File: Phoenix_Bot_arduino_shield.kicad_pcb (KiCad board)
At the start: 2 copper layers, 135.9 x 64.8 mm, 46 parts, among them J1 Analog_signal_male, J10 Ground, J11 Ground, J12 Ground, J13 12V_terminal, J14 PWN(10-5), J15 On Board Supply, J16 1x8 Male, J17 1x8 Male, J18 PWM_(6-1), J19 Analog_Pin_1, J2 Encoder_signal, J20 1x8 Female, J21 1x8 Female, J22 Serial, J23 ICSP, J24 Analog_Pin_2, J25 Digital_Pins, J27 Solenoid_terminal, J28 Solendoid_middle_terminal, J29 bottom_solenoid_terminal, J3 Servo_signal, J4 Analog_signal_female, J5 Analog_signal_power, J6 Servo_Power, J7 Encoder_Power, J8 Analog_Power_female, J9 Ground, q1 solenoid_1, q2 solenoid_4, q3 solenoid_3, q4 solenoid_5, q5 solenoid_3, q6 solenoid_6

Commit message: Added .gitignore, rescued old PCB file. Cleaned up repo to match .gitignore settings.
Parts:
- removed J10, J11: Ground, Pin_Headers:Pin_Header_Straight_1x06_Pitch2.54mm
- removed J12, J9: Ground, Pin_Headers:Pin_Header_Straight_1x08_Pitch2.54mm
- removed J5: Analog_signal_power, Pin_Headers:Pin_Header_Straight_1x08_Pitch2.54mm
- J2: value Encoder_signal -> Encoder_Signal; footprint Pin_Headers:Pin_Header_Straight_1x06_Pitch2.54mm -> Pin_Headers:Pin_Header_Straight_1x04_Pitch2.54mm
- J4: value Analog_signal_female -> Analog_signal_male
- J7: value Encoder_Power -> encoder_power; footprint Pin_Headers:Pin_Header_Straight_1x06_Pitch2.54mm -> Pin_Headers:Pin_Header_Straight_1x04_Pitch2.54mm
- J8: value Analog_Power_female -> encoder_ground; footprint Pin_Headers:Pin_Header_Straight_1x08_Pitch2.54mm -> Pin_Headers:Pin_Header_Straight_1x04_Pitch2.54mm
- moved J4 83.8 mm to (200.7, 116.2), turned to 270 degrees
- moved J8 59.2 mm to (188.6, 80.0), turned to 90 degrees
- moved J2 36.2 mm to (196.2, 74.9), turned to 270 degrees
- moved J1 34.3 mm to (161.3, 116.2), turned to 90 degrees
- moved R2 32.2 mm to (168.4, 67.3)
- moved D9 31.6 mm to (162.6, 67.3), turned to 180 degrees
- moved J7 28.6 mm to (188.6, 77.5)
- moved R1 8.09 mm to (179.8, 67.3)
- moved D8 6.82 mm to (174.7, 67.3), turned to 180 degrees
- moved J6 2.54 mm to (138.4, 81.3)
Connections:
- J18 pad 3: /Encoder_6 -> Net-(J18-Pad3)
- J18 pad 4: /Encoder_5 -> Net-(J18-Pad4)
- J18 pad 5: /Encoder_4 -> Net-(J18-Pad5)
- J18 pad 6: /Encoder_3 -> Net-(J18-Pad6)
- J18 pad 7: /Encoder_2 -> Net-(J18-Pad7)
- J18 pad 8: /Encoder_1 -> Net-(J18-Pad8)
- J22 pad 1: /SDA -> /Encoder_1
- J22 pad 2: /SCL -> /Encoder_2
- J22 pad 3: Net-(J22-Pad3) -> /Encoder_3
- J22 pad 4: Net-(J22-Pad4) -> /Encoder_4
- J7 pad 3: +5V -> Net-(J7-Pad3)
- J8 pad 1: +5V -> GND
- J8 pad 2: +5V -> GND
- J8 pad 3: Net-(J8-Pad3) -> GND
- J8 pad 4: +5V -> GND
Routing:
- net +12V: track 210.6 -> 0.00 mm
- net /Drain_2: track 55.1 -> 0.00 mm
- net /Drain_3: track 46.0 -> 0.00 mm
- net /Drain_6: track 35.6 -> 0.00 mm
- net /Drain_5: track 31.5 -> 0.00 mm
- net /Drain_1: track 26.3 -> 0.00 mm
- net /Drain_4: track 23.7 -> 0.00 mm
- net /TX: track 0.00 -> 8.91 mm
- net /RX: track 0.00 -> 4.54 mm
- net /Analog_9: track 0.00 -> 4.29 mm
- net /Encoder_3: track 0.00 -> 4.20 mm
- net /Encoder_4: track 0.00 -> 4.20 mm
- net /Encoder_1: track 0.00 -> 4.20 mm
- net /Encoder_2: track 0.00 -> 4.20 mm
- net /Analog_16: track 0.00 -> 3.70 mm
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- added copper zone on F.Cu, net +5V
- added copper zone on F.Cu, net Net-(D1-Pad2)
- added copper zone on F.Cu, net Net-(F1-Pad1)
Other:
- net class Default: clearance 0.006 -> 0.1524; trace_width 0.006 -> 0.1524; via_dia 0.027 -> 0.6858; via_drill 0.013 -> 0.3302
- net class Powertrace: clearance 0.006 -> 0.254; trace_width 0.0544 -> 1.38176; via_dia 0.027 -> 0.6858; via_drill 0.013 -> 0.3302
- rule trace_clearance: 0.006 -> 0.1524
- rule trace_min: 0.006 -> 0.1524
- rule via_min_drill: 0.013 -> 0.3302
- rule via_min_size: 0.027 -> 0.6858
- board text removed: "+"
- board text removed: "-"
- board text removed: "S"

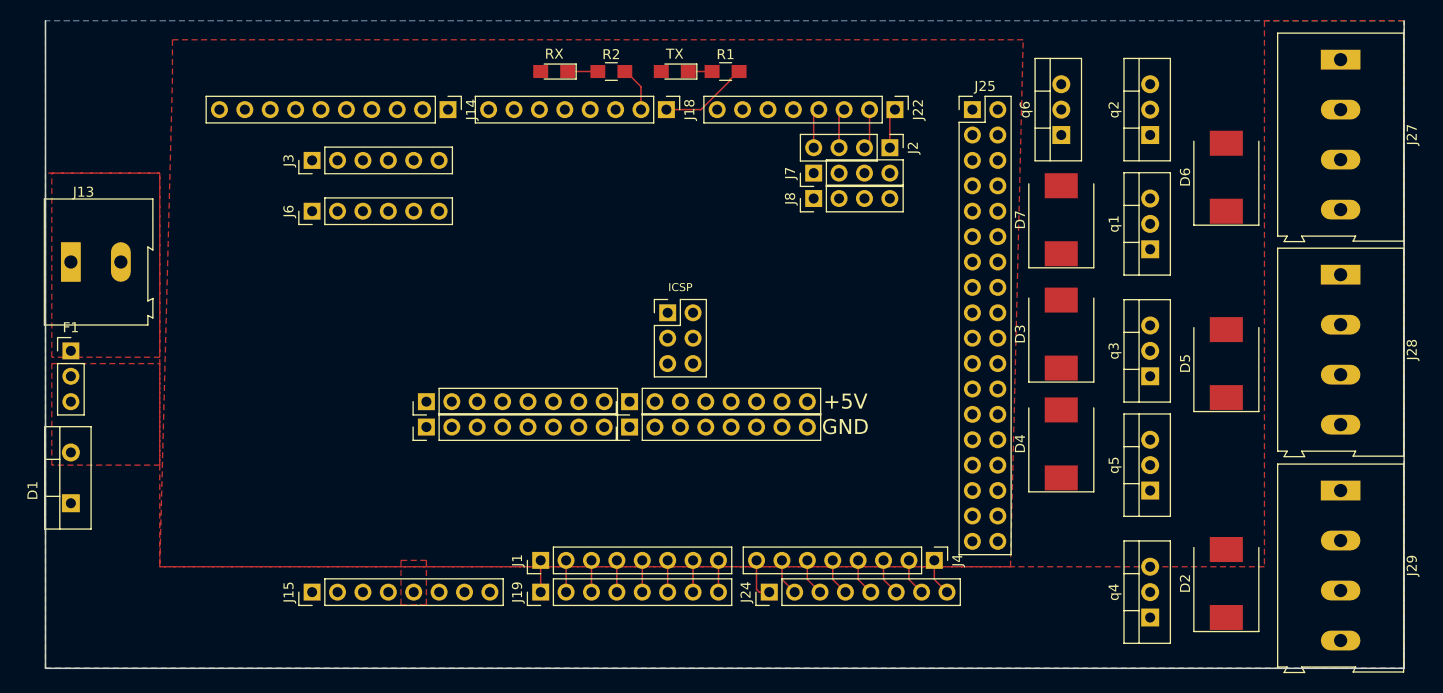
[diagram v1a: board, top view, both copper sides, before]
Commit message: Fixed issues porting from mac and started solenoid wiring
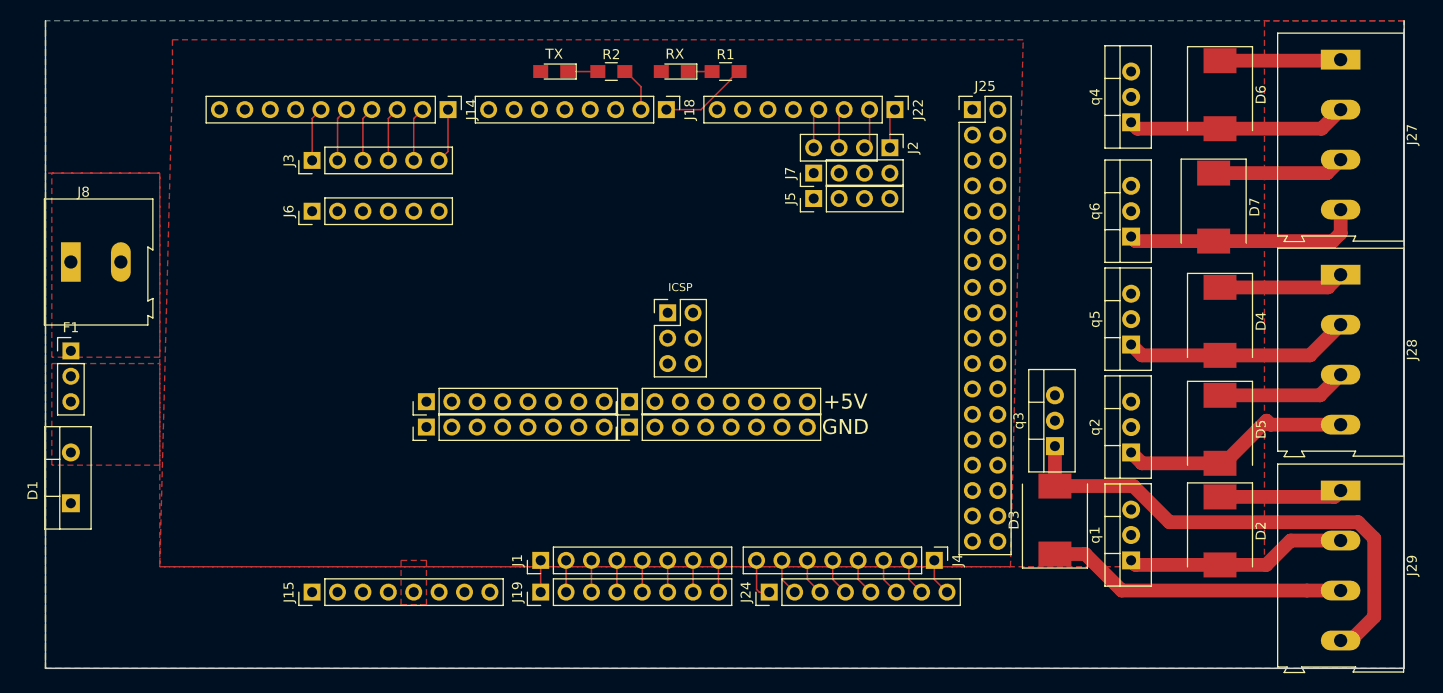
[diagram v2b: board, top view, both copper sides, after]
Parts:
- removed the J8 at (188.6, 80.0)
- added J5: encoder_power, Pin_Headers:Pin_Header_Straight_1x04_Pitch2.54mm, F.Cu at (188.6, 80.0)
- D8: value TX -> RX
- D9: value RX -> TX
- J4: value Analog_signal_male -> Analog_signal_female
- J6: value Servo_Power -> Servo_ground
- J7: value encoder_power -> encoder_ground
- moved q4 49.6 mm to (220.3, 72.4)
- moved q2 31.8 mm to (220.3, 105.4)
- moved q1 31.2 mm to (220.3, 116.2)
- moved D4 20.1 mm to (229.2, 92.3), turned to 270 degrees
- moved D3 18.6 mm to (212.7, 112.2)
- moved D7 15.3 mm to (228.6, 80.9), turned to 270 degrees
- moved q5 14.7 mm to (220.3, 94.6)
- moved q6 12.3 mm to (220.3, 83.8)
- moved q3 11.8 mm to (212.7, 104.8)
- moved D6 8.28 mm to (229.2, 69.6), turned to 270 degrees
- moved D5 6.61 mm to (229.2, 103.1), turned to 270 degrees
- moved D2 5.30 mm to (229.2, 113.3), turned to 270 degrees
- renumbered J13 to J8
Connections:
- J6 pad 1: +5V -> GND
- J6 pad 2: +5V -> GND
- J6 pad 3: +5V -> GND
- J6 pad 4: +5V -> GND
- J6 pad 5: +5V -> GND
- J6 pad 6: +5V -> GND
- J7 pad 1: +5V -> GND
- J7 pad 2: +5V -> GND
- J7 pad 3: Net-(J7-Pad3) -> GND
- J7 pad 4: +5V -> GND
- R1 pad 1: Net-(D8-Pad1) -> Net-(D9-Pad1)
- R2 pad 1: Net-(D9-Pad1) -> Net-(D8-Pad1)
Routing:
- net +12V: track 0.00 -> 93.3 mm
- net /Drain_2: track 0.00 -> 50.3 mm
- net /Drain_6: track 0.00 -> 23.8 mm
- net /Drain_4: track 0.00 -> 23.3 mm
- net /Drain_3: track 0.00 -> 22.7 mm
- net /Drain_1: track 0.00 -> 22.2 mm
- net /Drain_5: track 0.00 -> 22.0 mm
- net /Servo_6: track 0.00 -> 5.45 mm
- net /Servo_5: track 0.00 -> 5.45 mm
- net /Servo_3: track 0.00 -> 5.45 mm
- net /Servo_2: track 0.00 -> 5.45 mm
- net /Servo_4: track 0.00 -> 5.45 mm
- net /Servo_1: track 0.00 -> 5.45 mm

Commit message: Added my name, and finished solenoid mapping
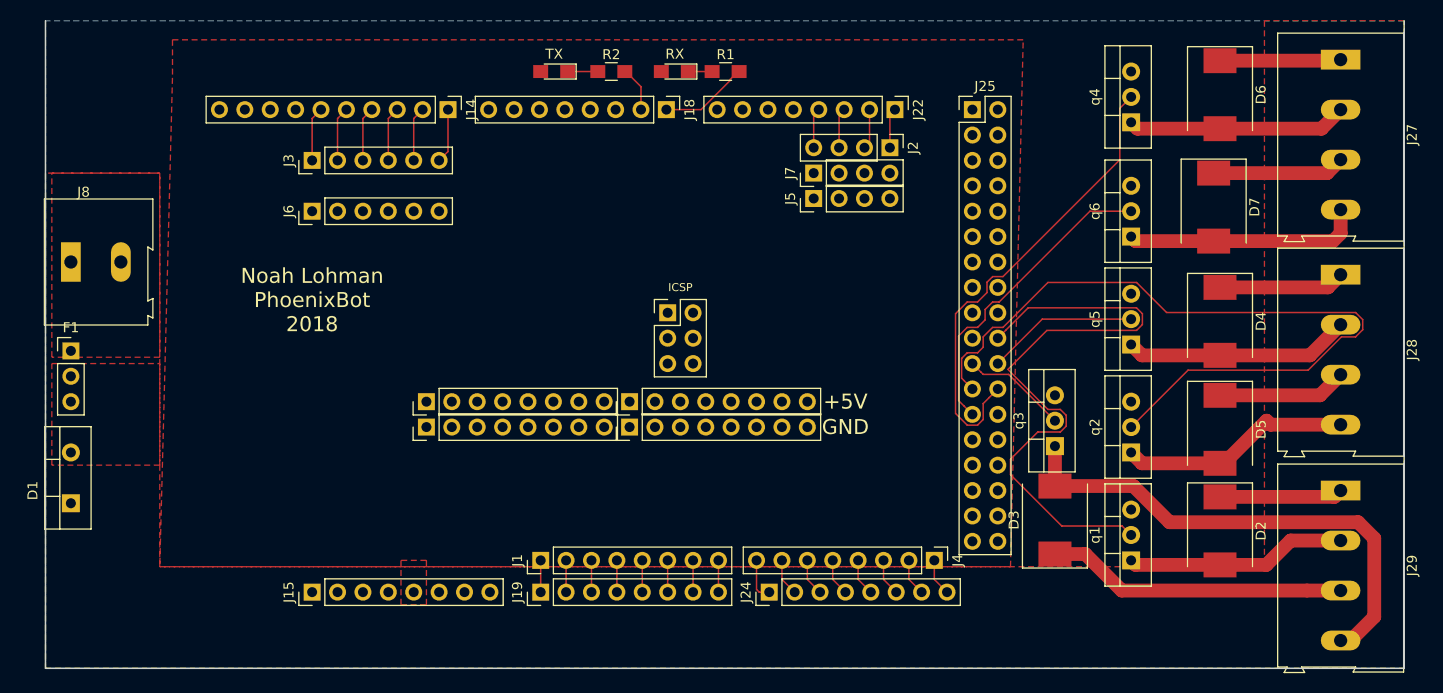
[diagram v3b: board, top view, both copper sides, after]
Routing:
- net /Ctrl_4: track 0.00 -> 77.1 mm
- net /Ctrl_1: track 0.00 -> 64.2 mm
- net /Ctrl_5: track 0.00 -> 47.3 mm
- net /Ctrl_6: track 0.00 -> 31.4 mm
- net /Ctrl_3: track 0.00 -> 15.2 mm
- net /Ctrl_2: track 0.00 -> 10.6 mm
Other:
- board text added: "Noah Lohman PhoenixBot 2018"
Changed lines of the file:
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@@
 (kicad_pcb (version 4) (host pcbnew 4.0.7)
   (general
-    (links 128)
-    (no_connects 38)
-    (area 111.684999 62.154999 247.725001 127.075001)
+    (links 126)
+    (no_connects 10)
+    (area 87.094287 50.64 249.579 127.849001)
     (thickness 1.6)
-    (drawings 9)
-    (tracks 106)
+    (drawings 10)
+    (tracks 178)
     (zones 0)
     (modules 41)
@@
   )
   (setup
-    (last_trace_width 1.38176)
+    (last_trace_width 0.1524)
     (user_trace_width 1.38176)
     (trace_clearance 0.1524)
@@
     )
   )
+  (gr_text "Noah Lohman\nPhoenixBot\n2018\n" (at 138.43 90.17) (layer F.SilkS)
+    (effects (font (size 1.5 1.5) (thickness 0.3)))
+  )
   (gr_text ICSP (at 175.26 88.9) (layer F.SilkS)
     (effects (font (size 0.8 0.8) (thickness 0.2)))
@@
   (segment (start 176.53 116.205) (end 176.53 119.38) (width 0.1524) (layer F.Cu) (net 7))
   (segment (start 179.07 119.38) (end 179.07 116.205) (width 0.1524) (layer F.Cu) (net 8))
+  (segment (start 220.345 113.665) (end 219.445001 112.765001) (width 0.1524) (layer F.Cu) (net 37))
+  (segment (start 219.445001 112.765001) (end 213.408519 112.765001) (width 0.1524) (layer F.Cu) (net 37))
+  (segment (start 208.023698 97.102632) (end 211.922729 93.203601) (width 0.1524) (layer F.Cu) (net 37))
+  (segment (start 213.408519 112.765001) (end 208.28 107.636482) (width 0.1524) (layer F.Cu) (net 37))
+  (segment (start 208.28 107.636482) (end 208.28 106.093128) (width 0.1524) (layer F.Cu) (net 37))
+  (segment (start 208.28 106.093128) (end 211.009527 103.363601) (width 0.1524) (layer F.Cu) (net 37))
+  (segment (start 211.009527 103.363601) (end 213.266729 103.363601) (width 0.1524) (layer F.Cu) (net 37))
+  (segment (start 210.043601 90.946399) (end 207.859999 93.130001) (width 0.1524) (layer F.Cu) (net 37))
+  (segment (start 213.266729 103.363601) (end 213.853601 102.776729) (width 0.1524) (layer F.Cu) (net 37))
+  (segment (start 213.853601 102.776729) (end 213.853601 101.693271) (width 0.1524) (layer F.Cu) (net 37))
+  (segment (start 213.853601 101.693271) (end 213.266729 101.106399) (width 0.1524) (layer F.Cu) (net 37))
+  (segment (start 213.266729 101.106399) (end 212.027465 101.106399) (width 0.1524) (layer F.Cu) (net 37))
+  (segment (start 212.027465 101.106399) (end 208.023698 97.102632) (width 0.1524) (layer F.Cu) (net 37))
+  (segment (start 211.922729 93.203601) (end 220.886729 93.203601) (width 0.1524) (layer F.Cu) (net 37))
+  (segment (start 207.859999 93.130001) (end 207.01 93.98) (width 0.1524) (layer F.Cu) (net 37))
+  (segment (start 220.886729 93.203601) (end 221.473601 92.616729) (width 0.1524) (layer F.Cu) (net 37))
+  (segment (start 221.473601 92.616729) (end 221.473601 91.533271) (width 0.1524) (layer F.Cu) (net 37))
+  (segment (start 221.473601 91.533271) (end 220.886729 90.946399) (width 0.1524) (layer F.Cu) (net 37))
+  (segment (start 220.886729 90.946399) (end 210.043601 90.946399) (width 0.1524) (layer F.Cu) (net 37))
+  (segment (start 212.725 102.235) (end 208.088601 97.598601) (width 0.1524) (layer F.Cu) (net 38))
+  (segment (start 208.088601 97.598601) (end 205.548601 97.598601) (width 0.1524) (layer F.Cu) (net 38))
+  (segment (start 205.548601 97.598601) (end 205.319999 97.369999) (width 0.1524) (layer F.Cu) (net 38))
+  (segment (start 205.319999 97.369999) (end 204.47 96.52) (width 0.1524) (layer F.Cu) (net 38))
+  (segment (start 220.345 92.075) (end 211.455 92.075) (width 0.1524) (layer F.Cu) (net 39))
+  (segment (start 211.455 92.075) (end 207.01 96.52) (width 0.1524) (layer F.Cu) (net 39))
+  (segment (start 220.345 102.87) (end 226.036399 97.178601) (width 0.1524) (layer F.Cu) (net 40))
+  (segment (start 226.036399 97.178601) (end 238.051754 97.178601) (width 0.1524) (layer F.Cu) (net 40))
+  (segment (start 205.548601 93.845069) (end 205.548601 94.880527) (width 0.1524) (layer F.Cu) (net 40))
+  (segment (start 238.051754 97.178601) (end 241.381745 93.84861) (width 0.1524) (layer F.Cu) (net 40))
+  (segment (start 241.381745 93.84861) (end 242.794764 93.84861) (width 0.1524) (layer F.Cu) (net 40))
+  (segment (start 242.794764 93.84861) (end 243.50861 93.134764) (width 0.1524) (layer F.Cu) (net 40))
+  (segment (start 203.620001 98.210001) (end 204.47 99.06) (width 0.1524) (layer F.Cu) (net 40))
+  (segment (start 243.50861 93.134764) (end 243.50861 92.125236) (width 0.1524) (layer F.Cu) (net 40))
+  (segment (start 243.50861 92.125236) (end 242.794764 91.41139) (width 0.1524) (layer F.Cu) (net 40))
+  (segment (start 203.391399 96.002271) (end 203.391399 97.981399) (width 0.1524) (layer F.Cu) (net 40))
+  (segment (start 242.794764 91.41139) (end 223.89172 91.41139) (width 0.1524) (layer F.Cu) (net 40))
+  (segment (start 207.527729 92.901399) (end 206.492271 92.901399) (width 0.1524) (layer F.Cu) (net 40))
+  (segment (start 223.89172 91.41139) (end 220.886729 88.406399) (width 0.1524) (layer F.Cu) (net 40))
+  (segment (start 204.987729 95.441399) (end 203.952271 95.441399) (width 0.1524) (layer F.Cu) (net 40))
+  (segment (start 220.886729 88.406399) (end 212.022729 88.406399) (width 0.1524) (layer F.Cu) (net 40))
+  (segment (start 212.022729 88.406399) (end 207.527729 92.901399) (width 0.1524) (layer F.Cu) (net 40))
+  (segment (start 206.492271 92.901399) (end 205.548601 93.845069) (width 0.1524) (layer F.Cu) (net 40))
+  (segment (start 205.548601 94.880527) (end 204.987729 95.441399) (width 0.1524) (layer F.Cu) (net 40))
+  (segment (start 203.952271 95.441399) (end 203.391399 96.002271) (width 0.1524) (layer F.Cu) (net 40))
+  (segment (start 203.391399 97.981399) (end 203.620001 98.210001) (width 0.1524) (layer F.Cu) (net 40))
+  (segment (start 220.345 69.85) (end 219.216399 70.978601) (width 0.1524) (layer F.Cu) (net 41))
+  (segment (start 219.216399 70.978601) (end 219.216399 76.132729) (width 0.1524) (layer F.Cu) (net 41))
+  (segment (start 219.216399 76.132729) (end 207.527729 87.821399) (width 0.1524) (layer F.Cu) (net 41))
+  (segment (start 206.160001 99.909999) (end 207.01 99.06) (width 0.1524) (layer F.Cu) (net 41))
+  (segment (start 207.527729 87.821399) (end 206.492271 87.821399) (width 0.1524) (layer F.Cu) (net 41))
+  (segment (start 206.492271 87.821399) (end 205.931399 88.382271) (width 0.1524) (layer F.Cu) (net 41))
+  (segment (start 202.78178 101.50811) (end 203.952271 102.678601) (width 0.1524) (layer F.Cu) (net 41))
+  (segment (start 205.931399 88.382271) (end 205.931399 89.417729) (width 0.1524) (layer F.Cu) (net 41))
+  (segment (start 205.931399 89.417729) (end 204.987729 90.361399) (width 0.1524) (layer F.Cu) (net 41))
+  (segment (start 204.987729 90.361399) (end 203.952271 90.361399) (width 0.1524) (layer F.Cu) (net 41))
+  (segment (start 203.952271 90.361399) (end 202.78178 91.53189) (width 0.1524) (layer F.Cu) (net 41))
+  (segment (start 202.78178 91.53189) (end 202.78178 101.50811) (width 0.1524) (layer F.Cu) (net 41))
+  (segment (start 205.548601 100.521399) (end 206.160001 99.909999) (width 0.1524) (layer F.Cu) (net 41))
+  (segment (start 203.952271 102.678601) (end 204.987729 102.678601) (width 0.1524) (layer F.Cu) (net 41))
+  (segment (start 204.987729 102.678601) (end 205.548601 102.117729) (width 0.1524) (layer F.Cu) (net 41))
+  (segment (start 205.548601 102.117729) (end 205.548601 100.521399) (width 0.1524) (layer F.Cu) (net 41))
+  (segment (start 220.345 81.28) (end 216.22633 81.28) (width 0.1524) (layer F.Cu) (net 42))
+  (segment (start 216.22633 81.28) (end 207.144931 90.361399) (width 0.1524) (layer F.Cu) (net 42))
+  (segment (start 207.144931 90.361399) (end 206.492271 90.361399) (width 0.1524) (layer F.Cu) (net 42))
+  (segment (start 205.74 92.149128) (end 204.987729 92.901399) (width 0.1524) (layer F.Cu) (net 42))
+  (segment (start 206.492271 90.361399) (end 205.74 91.11367) (width 0.1524) (layer F.Cu) (net 42))
+  (segment (start 203.952271 92.901399) (end 203.086589 93.767081) (width 0.1524) (layer F.Cu) (net 42))
+  (segment (start 205.74 91.11367) (end 205.74 92.149128) (width 0.1524) (layer F.Cu) (net 42))
+  (segment (start 204.987729 92.901399) (end 203.952271 92.901399) (width 0.1524) (layer F.Cu) (net 42))
+  (segment (start 203.086589 93.767081) (end 203.086589 100.216589) (width 0.1524) (layer F.Cu) (net 42))
+  (segment (start 203.086589 100.216589) (end 203.620001 100.750001) (width 0.1524) (layer F.Cu) (net 42))
+  (segment (start 203.620001 100.750001) (end 204.47 101.6) (width 0.1524) (layer F.Cu) (net 42))
   (segment (start 212.725 115.57) (end 215.75676 115.57) (width 1.38176) (layer F.Cu) (net 53))
   (segment (start 215.75676 115.57) (end 219.40676 119.22) (width 1.38176) (layer F.Cu) (net 53))
